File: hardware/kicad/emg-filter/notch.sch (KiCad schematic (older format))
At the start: 72 parts, among them U11 LM4565, U12 LM4565, U13 LM4565, U14 LM4565, U15 LM4565, U16 LM4565, U17 LM4565, U18 LM4565

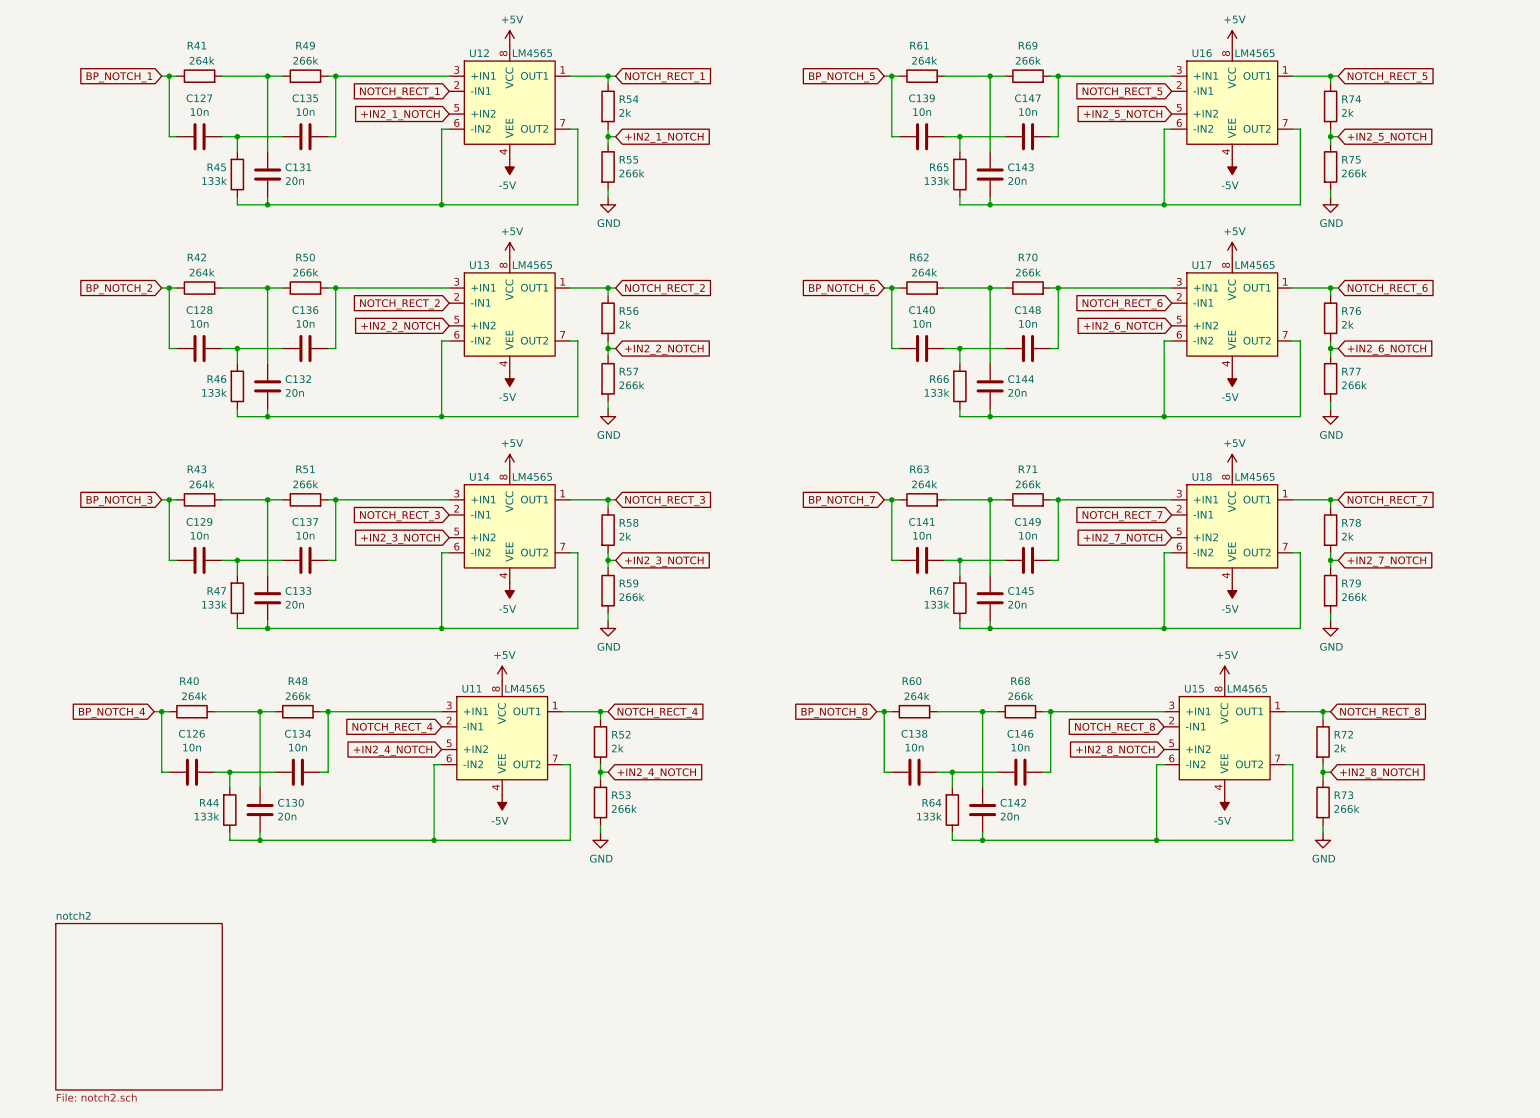
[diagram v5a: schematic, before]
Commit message: slip 264k and 266k, now 2x132k and 2x133k
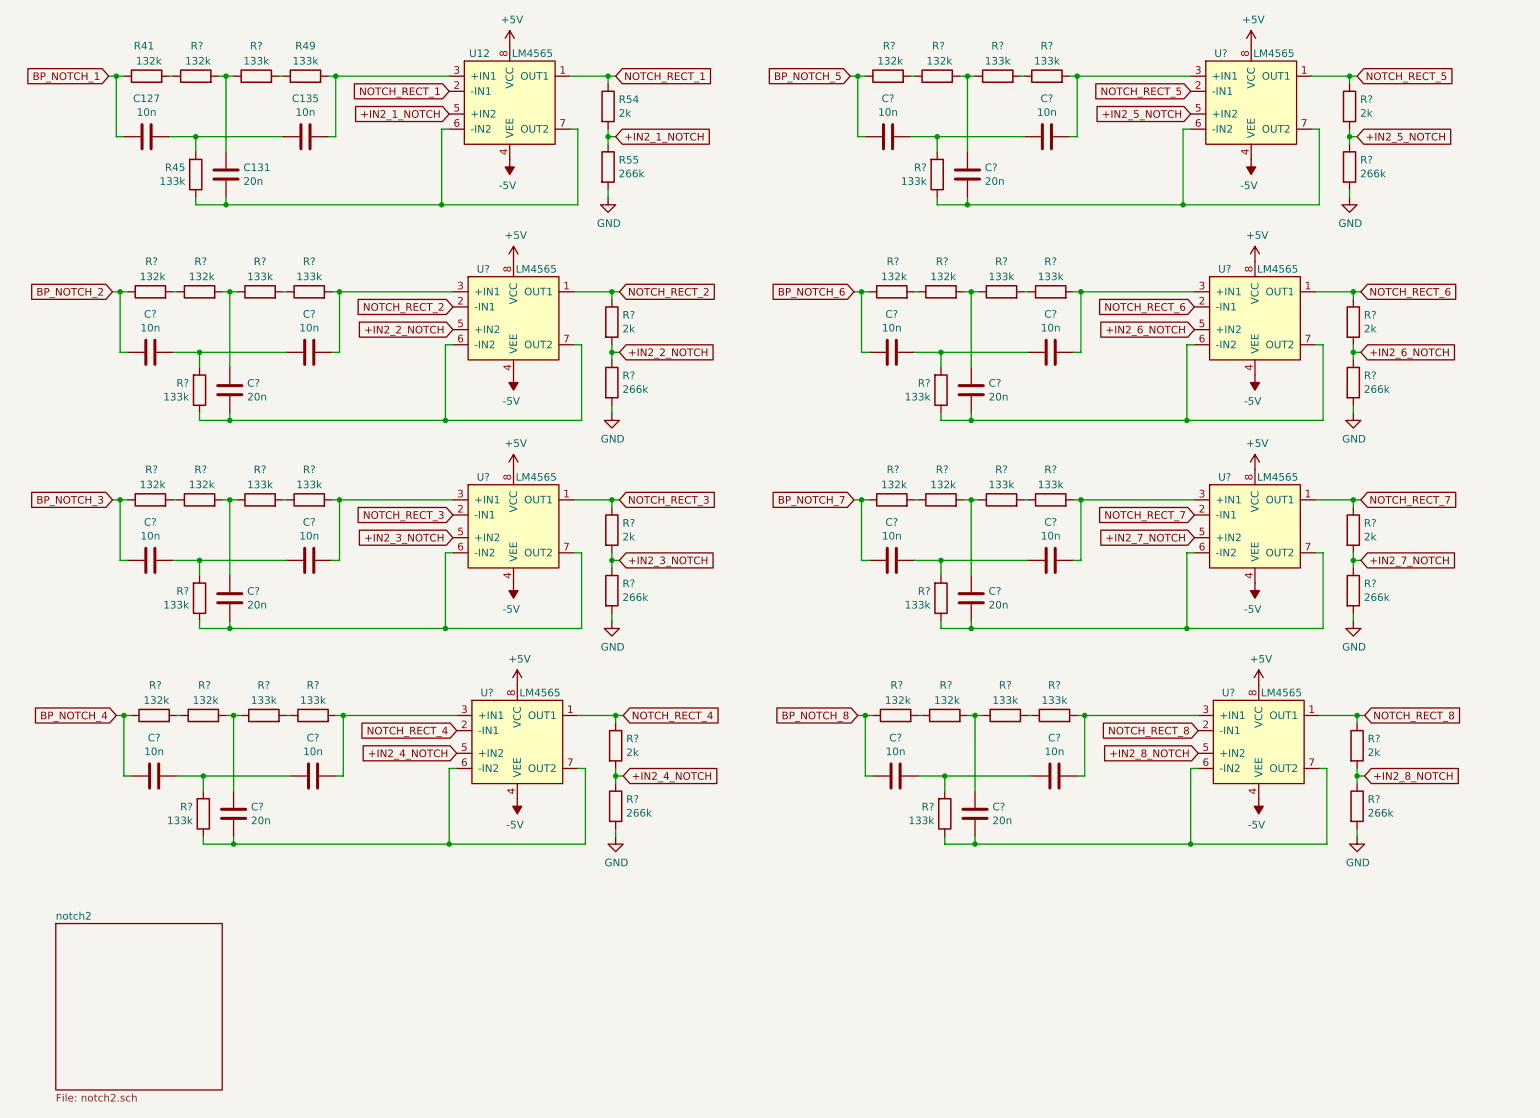
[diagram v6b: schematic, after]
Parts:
- removed C126, C128, C129, C134, C136, C137, C138, C139, C140, C141, C146, C147, C148, C149: 10n, Capacitor_SMD:C_0805_2012Metric, symbol Device:C
- removed C130, C132, C133, C142, C143, C144, C145: 20n, Capacitor_SMD:C_0805_2012Metric, symbol Device:C
- removed R40, R42, R43, R60, R61, R62, R63: 264k, Resistor_SMD:R_0805_2012Metric, symbol Device:R
- removed R44, R46, R47, R64, R65, R66, R67: 133k, Resistor_SMD:R_0805_2012Metric, symbol Device:R
- removed R48, R50, R51, R53, R57, R59, R68, R69, R70, R71, R73, R75, R77, R79: 266k, Resistor_SMD:R_0805_2012Metric, symbol Device:R
- removed R52, R56, R58, R72, R74, R76, R78: 2k, Resistor_SMD:R_0805_2012Metric, symbol Device:R
- removed U11, U13, U14, U15, U16, U17, U18: LM4565, symbol emg-filter:LM4565
- added C? (x7): 20n, Capacitor_SMD:C_0805_2012Metric, symbol Device:C
- added C? (x14): 10n, Capacitor_SMD:C_0805_2012Metric, symbol Device:C
- added R? (x15): 132k, Resistor_SMD:R_0805_2012Metric, symbol Device:R
- added R? (x22): 133k, Resistor_SMD:R_0805_2012Metric, symbol Device:R
- added R? (x7): 2k, Resistor_SMD:R_0805_2012Metric, symbol Device:R
- added R? (x7): 266k, Resistor_SMD:R_0805_2012Metric, symbol Device:R
- added U? (x7): LM4565, symbol emg-filter:LM4565
- R41: value 264k -> 132k
- R49: value 266k -> 133k
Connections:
- net +5V: now also U?.8 (VCC), U?.8 (VCC), U?.8 (VCC), U?.8 (VCC), U?.8 (VCC), U?.8 (VCC), U?.8 (VCC)
- net +IN2_2_NOTCH: now also R?.1, R?.2, U?.5 (+IN2)
- net +IN2_3_NOTCH: now also R?.1, R?.2, U?.5 (+IN2)
- net +IN2_4_NOTCH: now also R?.1, R?.2, U?.5 (+IN2)
- net +IN2_5_NOTCH: now also R?.1, R?.2, U?.5 (+IN2)
- net +IN2_6_NOTCH: now also R?.1, R?.2, U?.5 (+IN2)
- net +IN2_7_NOTCH: now also R?.1, R?.2, U?.5 (+IN2)
- net +IN2_8_NOTCH: now also R?.1, R?.2, U?.5 (+IN2)
- net -5V: now also U?.4 (VEE), U?.4 (VEE), U?.4 (VEE), U?.4 (VEE), U?.4 (VEE), U?.4 (VEE), U?.4 (VEE)
- net BP_NOTCH_2: now also C?.2, R?.1
- net BP_NOTCH_3: now also C?.2, R?.1
- net BP_NOTCH_4: now also C?.2, R?.1
- net BP_NOTCH_5: now also C?.2, R?.1
- net BP_NOTCH_6: now also C?.2, R?.1
- net BP_NOTCH_7: now also C?.2, R?.1
- net BP_NOTCH_8: now also C?.2, R?.1
- net GND: now also R?.2, R?.2, R?.2, R?.2, R?.2, R?.2, R?.2
- net NOTCH_RECT_2: now also R?.1, U?.1 (OUT1), U?.2 (-IN1)
- net NOTCH_RECT_3: now also R?.1, U?.1 (OUT1), U?.2 (-IN1)
- net NOTCH_RECT_4: now also R?.1, U?.1 (OUT1), U?.2 (-IN1)
- net NOTCH_RECT_5: now also R?.1, U?.1 (OUT1), U?.2 (-IN1)
- net NOTCH_RECT_6: now also R?.1, U?.1 (OUT1), U?.2 (-IN1)
- net NOTCH_RECT_7: now also R?.1, U?.1 (OUT1), U?.2 (-IN1)
- net NOTCH_RECT_8: now also R?.1, U?.1 (OUT1), U?.2 (-IN1)
- new net: R41.2, R?.1
- new net: R49.1, R?.2
- new net: C131.2, R?.1, R?.2
- new net: C?.1, R?.2, U?.3 (+IN1) (x7)
- new net: C?.1, R?.1, U?.6 (-IN2), U?.7 (OUT2) (x7)
- new net: R?.1, R?.2 (x14)
- new net: C?.1, C?.2, R?.2 (x7)
- new net: C?.2, R?.1, R?.2 (x7)
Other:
- moved on the sheet: C127, C131, R41, R45

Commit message: Solving Stuff for Free
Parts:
- gave numbers to parts that had none: 79
- renumbered C127 to C126, C131 to C130, C135 to C134, R41 to R40, R49 to R56, R54 to R60, R55 to R61, U12 to U11
